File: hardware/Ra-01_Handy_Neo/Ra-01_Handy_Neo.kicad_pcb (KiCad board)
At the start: 4 copper layers, 68.6 x 53.3 mm, 35 parts, among them J1 Power, J2 Digital/PWM, J3 Analog, J4 Digital/PWM, J5 Conn_Coaxial, J6 Conn_01x04_Pin, SW1 SW_Push, SW10 SW_Push, SW11 SW_Push, SW12 SW_Push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

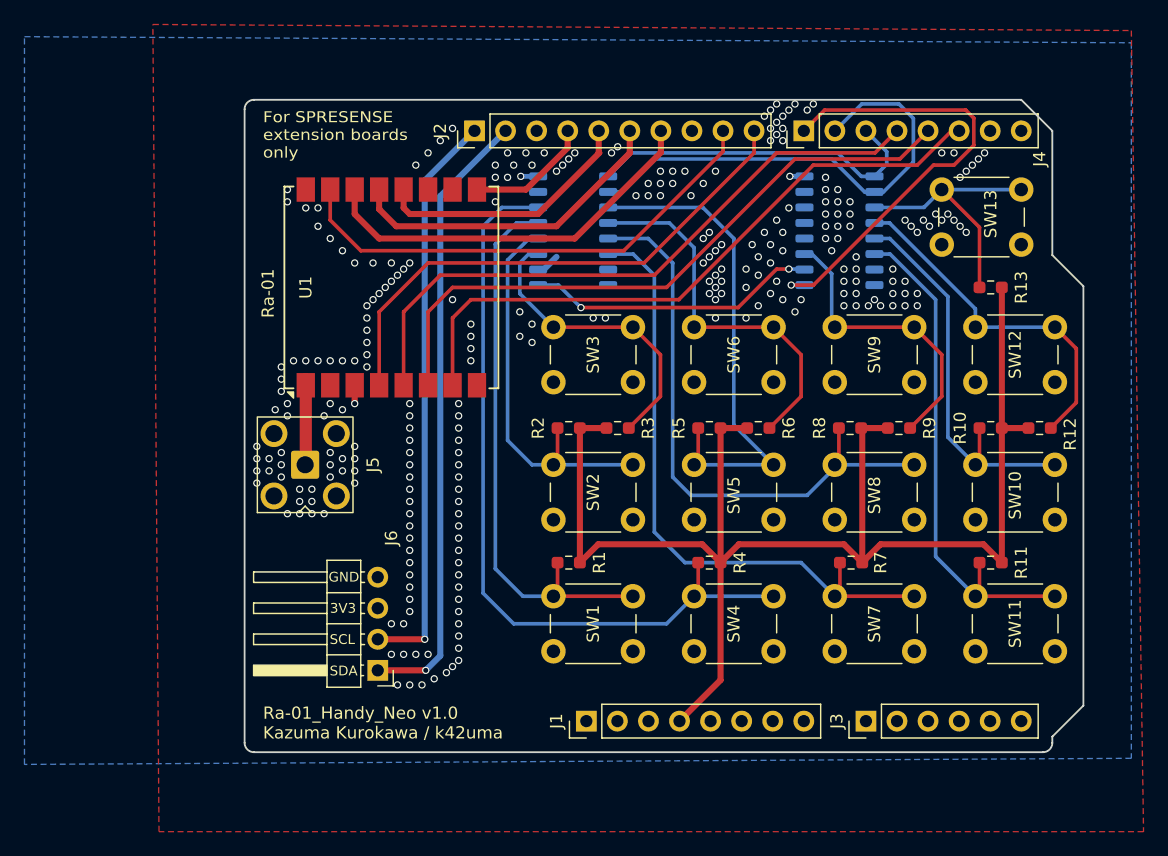
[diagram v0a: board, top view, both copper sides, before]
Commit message: change footprints and 3dsymbols to export step file
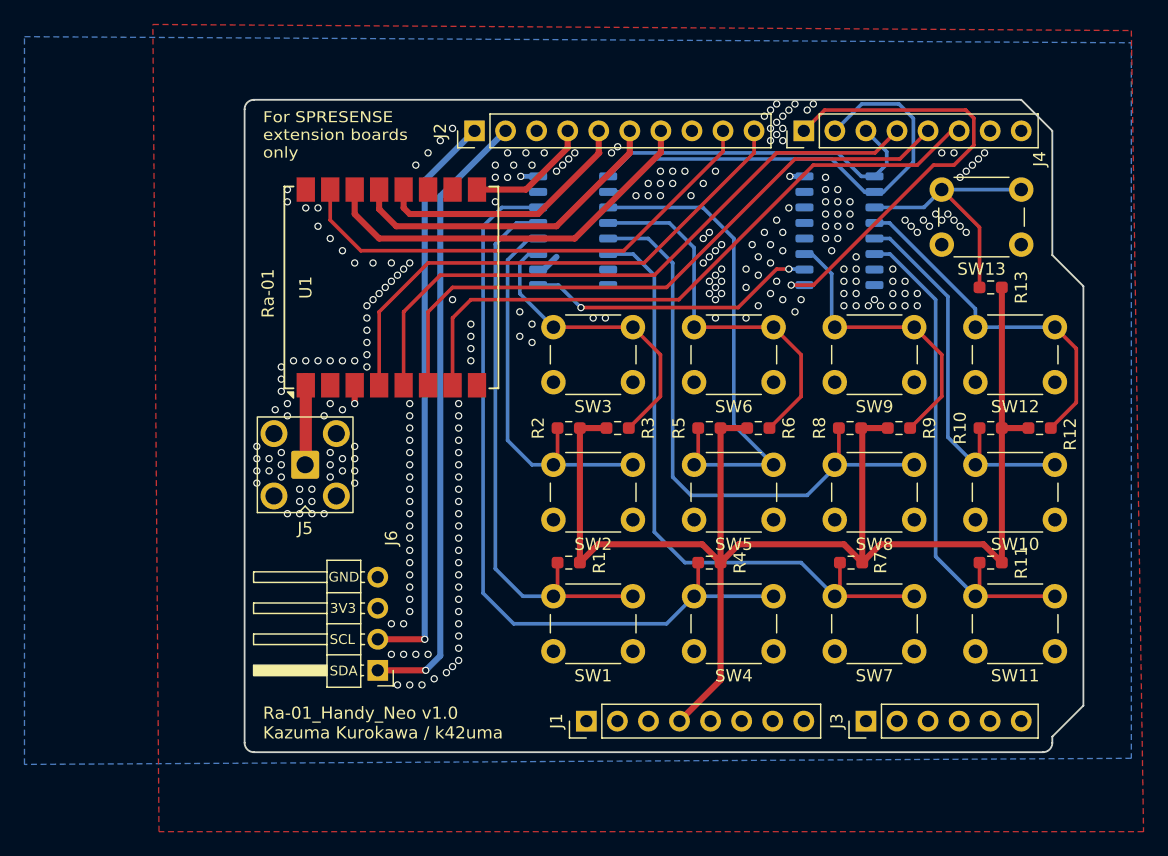
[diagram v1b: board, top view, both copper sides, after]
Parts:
- J5: footprint Connector_Coaxial:SMA_BAT_Wireless_BWSMA-KWE-Z001 -> Connector_Coaxial:SMA_Connector_at_Honbu_3-1478978-1
- SW1, SW10, SW11, SW12, SW13, SW2, SW3, SW4, SW5, SW6, SW7, SW8, SW9: footprint Button_Switch_THT:SW_PUSH_6mm_H5mm -> Button_Switch_THT:SW_PUSH_6mm_H6.5mm
